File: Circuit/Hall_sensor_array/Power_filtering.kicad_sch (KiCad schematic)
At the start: 1 part, among them U275 LM1117-3.3

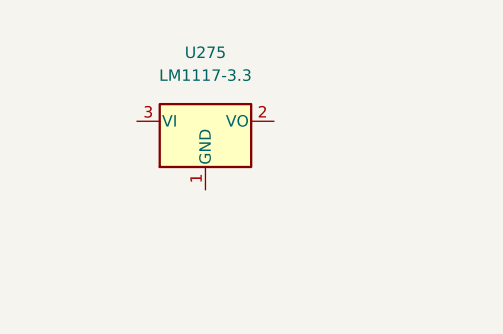
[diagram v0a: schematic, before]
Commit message: Updated circuit
Added binary counter for selecting analog multiplexer address
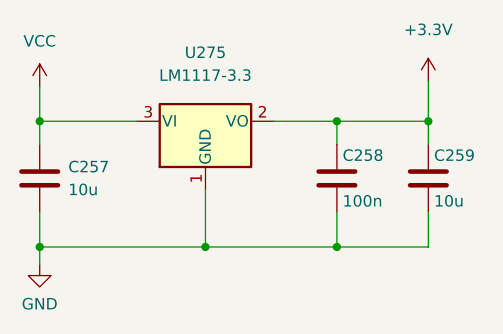
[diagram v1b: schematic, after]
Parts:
- added C257, C259: 10u, symbol Device:C
- added C258: 100n, symbol Device:C
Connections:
- net GND: now reaches U275.1 (GND)
- net GND: now also C257.2, C258.2, C259.2
- net +3.3V: now reaches U275.2 (VO)
- net +3.3V: now also C258.1, C259.1
- net VCC: now reaches U275.3 (VI)
- net VCC: now also C257.1
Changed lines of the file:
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@@
 (kicad_sch (version 20211123) (generator eeschema)
   (paper "A4")
+  (junction (at 38.735 52.07) (diameter 0) (color 0 0 0 0)
+  )
+  (junction (at 71.755 66.04) (diameter 0) (color 0 0 0 0)
+  )
+  (junction (at 81.915 52.07) (diameter 0) (color 0 0 0 0)
+  )
+  (junction (at 38.735 66.04) (diameter 0) (color 0 0 0 0)
+  )
+  (junction (at 57.15 66.04) (diameter 0) (color 0 0 0 0)
+  )
+  (junction (at 71.755 52.07) (diameter 0) (color 0 0 0 0)
+  )
+  (wire (pts (xy 71.755 66.04) (xy 57.15 66.04))
+    (stroke (width 0) (type default) (color 0 0 0 0))
+  )
+  (wire (pts (xy 81.915 62.23) (xy 81.915 66.04))
+    (stroke (width 0) (type default) (color 0 0 0 0))
+  )
+  (wire (pts (xy 38.735 62.23) (xy 38.735 66.04))
+    (stroke (width 0) (type default) (color 0 0 0 0))
+  )
+  (wire (pts (xy 71.755 62.23) (xy 71.755 66.04))
+    (stroke (width 0) (type default) (color 0 0 0 0))
+  )
+  (wire (pts (xy 81.915 66.04) (xy 71.755 66.04))
+    (stroke (width 0) (type default) (color 0 0 0 0))
+  )
+  (wire (pts (xy 38.735 66.04) (xy 38.735 67.945))
+    (stroke (width 0) (type default) (color 0 0 0 0))
+  )
+  (wire (pts (xy 57.15 66.04) (xy 38.735 66.04))
+    (stroke (width 0) (type default) (color 0 0 0 0))
+  )
+  (wire (pts (xy 71.755 52.07) (xy 64.77 52.07))
+    (stroke (width 0) (type default) (color 0 0 0 0))
+  )
+  (wire (pts (xy 81.915 52.07) (xy 71.755 52.07))
+    (stroke (width 0) (type default) (color 0 0 0 0))
+  )
+  (wire (pts (xy 81.915 47.625) (xy 81.915 52.07))
+    (stroke (width 0) (type default) (color 0 0 0 0))
+  )
+  (wire (pts (xy 71.755 54.61) (xy 71.755 52.07))
+    (stroke (width 0) (type default) (color 0 0 0 0))
+  )
+  (wire (pts (xy 38.735 52.07) (xy 49.53 52.07))
+    (stroke (width 0) (type default) (color 0 0 0 0))
+  )
+  (wire (pts (xy 38.735 48.26) (xy 38.735 52.07))
+    (stroke (width 0) (type default) (color 0 0 0 0))
+  )
+  (wire (pts (xy 81.915 54.61) (xy 81.915 52.07))
+    (stroke (width 0) (type default) (color 0 0 0 0))
+  )
+  (wire (pts (xy 38.735 52.07) (xy 38.735 54.61))
+    (stroke (width 0) (type default) (color 0 0 0 0))
+  )
+  (wire (pts (xy 57.15 59.69) (xy 57.15 66.04))
+    (stroke (width 0) (type default) (color 0 0 0 0))
+  )
+  (symbol (lib_id "Device:C") (at 71.755 58.42 0) (unit 1)
+    (in_bom yes) (on_board yes)
+    (property "Reference" "C258" (id 0) (at 72.39 55.88 0)
+      (effects (font (size 1.27 1.27)) (justify left))
+    )
+    (property "Value" "100n" (id 1) (at 72.39 60.96 0)
+      (effects (font (size 1.27 1.27)) (justify left))
+    )
+    (property "Footprint" "" (id 2) (at 72.7202 62.23 0)
+      (effects (font (size 1.27 1.27)) hide)
+    )
+    (property "Datasheet" "~" (id 3) (at 71.755 58.42 0)
+      (effects (font (size 1.27 1.27)) hide)
+    )
+    (pin "1")
+    (pin "2")
+  )
+  (symbol (lib_id "power:+3.3V") (at 81.915 47.625 0) (unit 1)
+    (in_bom yes) (on_board yes) (fields_autoplaced)
+    (property "Reference" "#PWR?" (id 0) (at 81.915 51.435 0)
+      (effects (font (size 1.27 1.27)) hide)
+    )
+    (property "Value" "+3.3V" (id 1) (at 81.915 41.91 0))
+    (property "Footprint" "" (id 2) (at 81.915 47.625 0)
+      (effects (font (size 1.27 1.27)) hide)
+    )
+    (property "Datasheet" "" (id 3) (at 81.915 47.625 0)
+      (effects (font (size 1.27 1.27)) hide)
+    )
+    (pin "1")
+  )
   (symbol (lib_id "Regulator_Linear:LM1117-3.3") (at 57.15 52.07 0) (unit 1)
     (in_bom yes) (on_board yes) (fields_autoplaced)
@@
     (pin "3")
   )
+  (symbol (lib_id "Device:C") (at 38.735 58.42 0) (unit 1)
+    (in_bom yes) (on_board yes) (fields_autoplaced)
+    (property "Reference" "C257" (id 0) (at 41.91 57.1499 0)
+      (effects (font (size 1.27 1.27)) (justify left))
+    )
+    (property "Value" "10u" (id 1) (at 41.91 59.6899 0)
+      (effects (font (size 1.27 1.27)) (justify left))
+    )
+    (property "Footprint" "" (id 2) (at 39.7002 62.23 0)
+      (effects (font (size 1.27 1.27)) hide)
+    )
+    (property "Datasheet" "~" (id 3) (at 38.735 58.42 0)
+      (effects (font (size 1.27 1.27)) hide)
+    )
+    (pin "1")
+    (pin "2")
+  )
+  (symbol (lib_id "power:GND") (at 38.735 67.945 0) (unit 1)
+    (in_bom yes) (on_board yes) (fields_autoplaced)
+    (property "Reference" "#PWR0645" (id 0) (at 38.735 74.295 0)
+      (effects (font (size 1.27 1.27)) hide)
+    )
+    (property "Value" "GND" (id 1) (at 38.735 72.39 0))
+    (property "Footprint" "" (id 2) (at 38.735 67.945 0)
+      (effects (font (size 1.27 1.27)) hide)
+    )
+    (property "Datasheet" "" (id 3) (at 38.735 67.945 0)
+      (effects (font (size 1.27 1.27)) hide)
+    )
+    (pin "1")
+  )
+  (symbol (lib_id "Device:C") (at 81.915 58.42 0) (unit 1)
+    (in_bom yes) (on_board yes)
+    (property "Reference" "C259" (id 0) (at 82.55 55.88 0)
+      (effects (font (size 1.27 1.27)) (justify left))
+    )
+    (property "Value" "10u" (id 1) (at 82.55 60.96 0)
+      (effects (font (size 1.27 1.27)) (justify left))
+    )
+    (property "Footprint" "" (id 2) (at 82.8802 62.23 0)
+      (effects (font (size 1.27 1.27)) hide)
+    )
+    (property "Datasheet" "~" (id 3) (at 81.915 58.42 0)
+      (effects (font (size 1.27 1.27)) hide)
+    )
+    (pin "1")
+    (pin "2")
+  )
+  (symbol (lib_id "power:VCC") (at 38.735 48.26 0) (unit 1)
+    (in_bom yes) (on_board yes) (fields_autoplaced)
+    (property "Reference" "#PWR0647" (id 0) (at 38.735 52.07 0)
+      (effects (font (size 1.27 1.27)) hide)
+    )
+    (property "Value" "VCC" (id 1) (at 38.735 43.18 0))
+    (property "Footprint" "" (id 2) (at 38.735 48.26 0)
+      (effects (font (size 1.27 1.27)) hide)
+    )
+    (property "Datasheet" "" (id 3) (at 38.735 48.26 0)
+      (effects (font (size 1.27 1.27)) hide)
+    )
+    (pin "1")
+  )
 )
